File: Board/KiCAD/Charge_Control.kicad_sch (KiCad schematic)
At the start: 56 parts, among them Q1 AON7408, Q10 AON7407, Q2 AON7408, Q3 AON7408, Q4 AON7408, U1 BQ25730RSNR, U3 LTC2943CDD#PBF

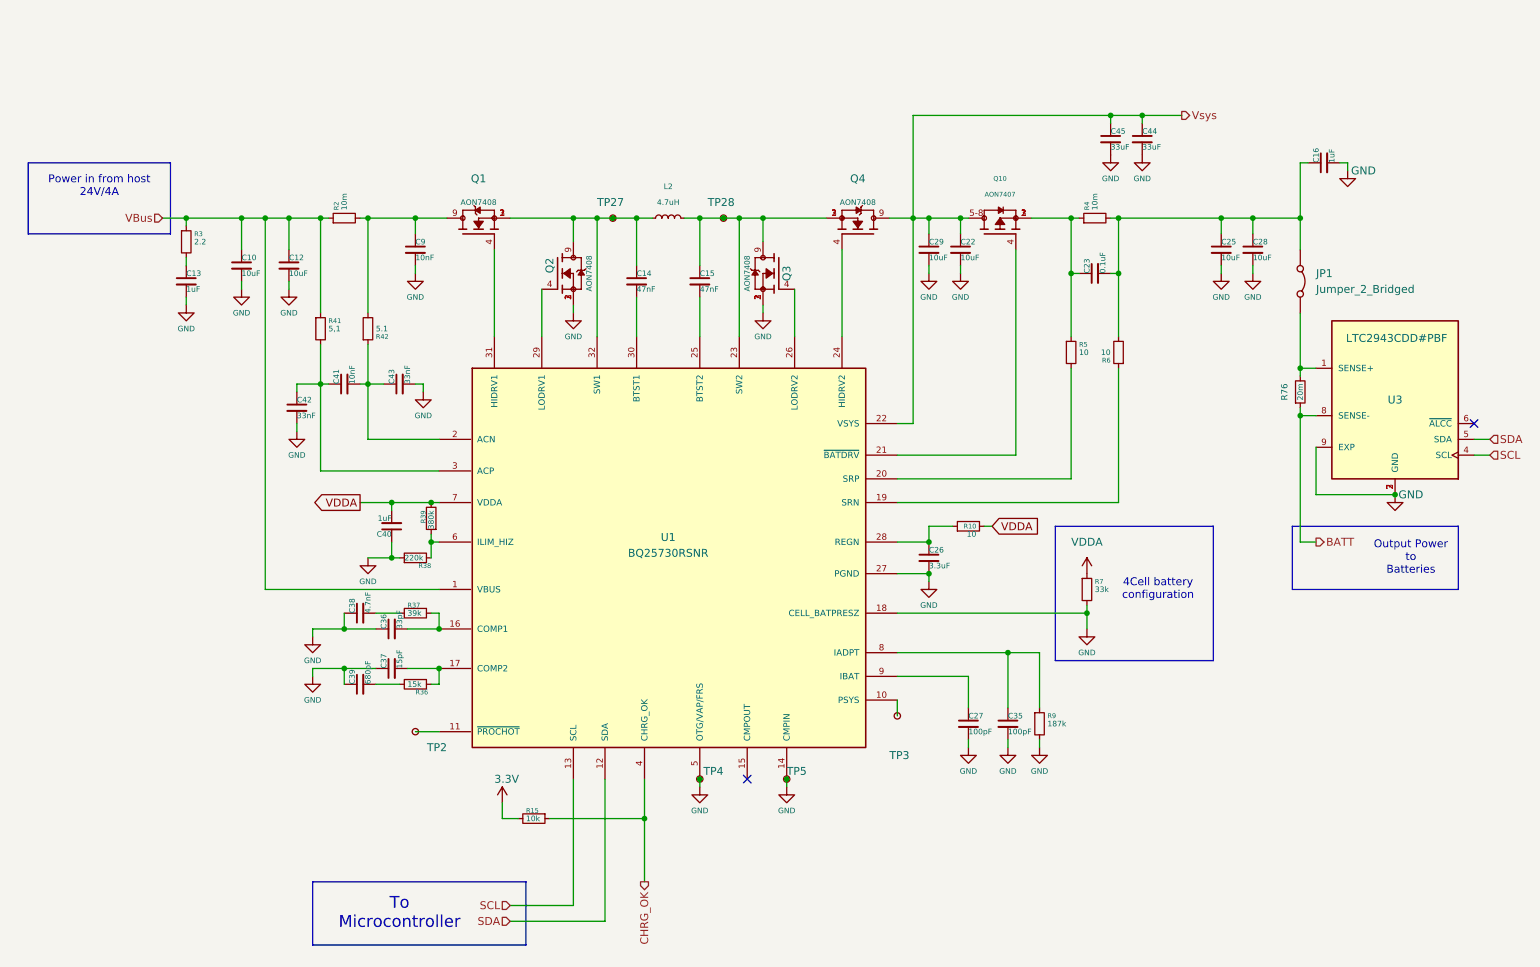
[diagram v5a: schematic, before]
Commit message: Started updating BOM with MFR/MPN
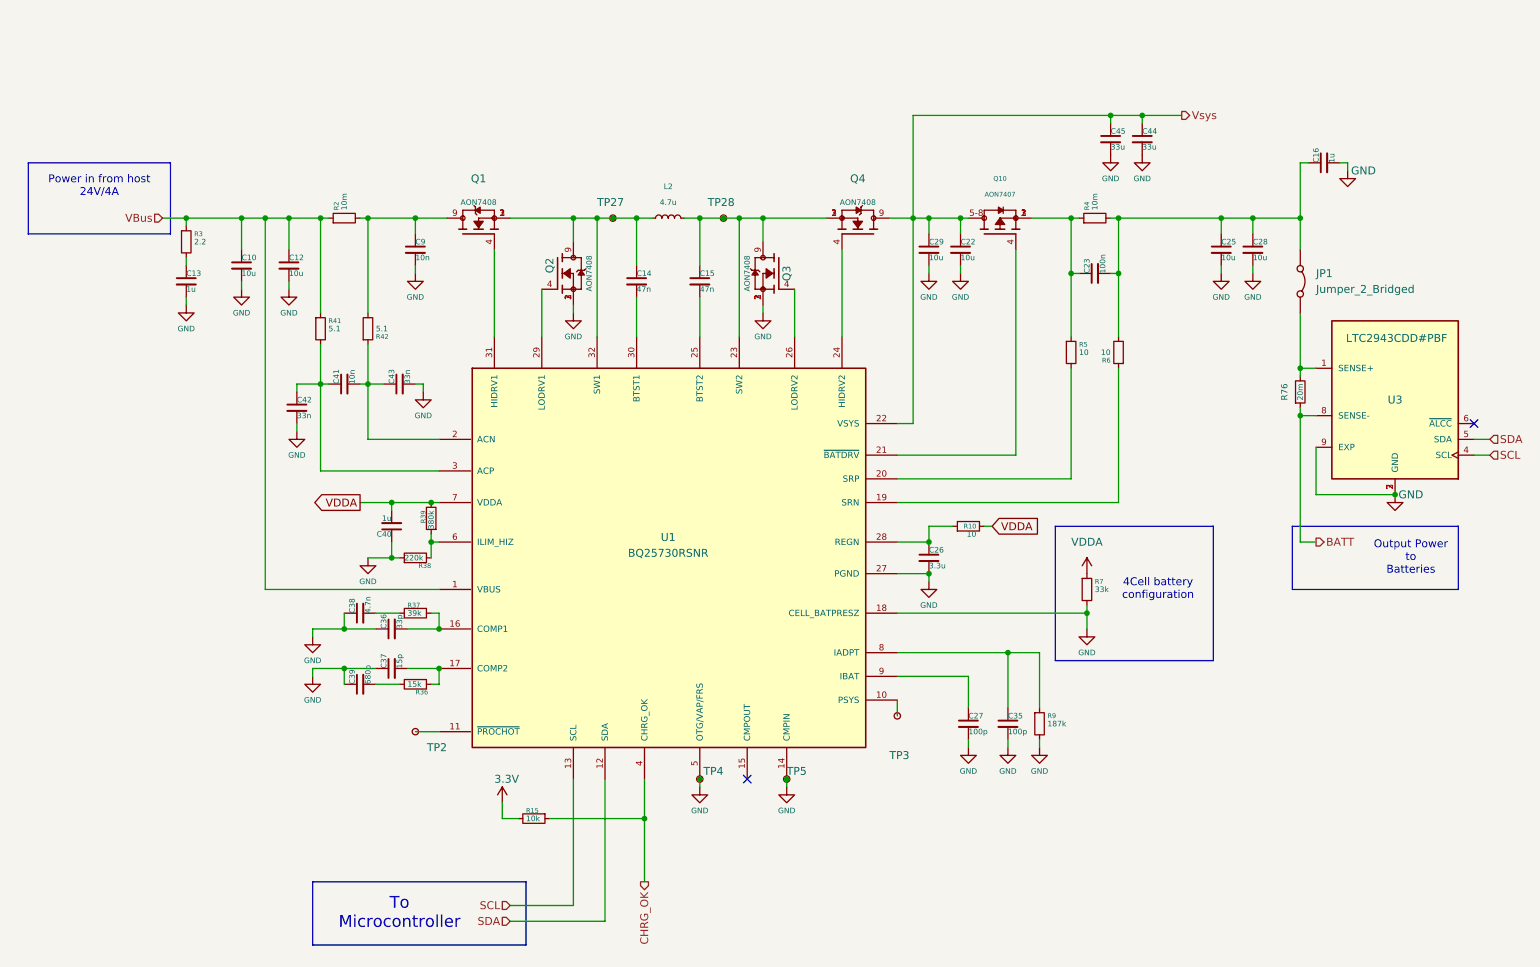
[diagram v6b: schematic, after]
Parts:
- C10, C12, C22, C25, C28, C29: value 10uF -> 10u
- C13, C16, C40: value 1uF -> 1u
- C14, C15: value 47nF -> 47n
- C23: value 0.1uF -> 100n
- C26: value 3.3uF -> 3.3u
- C27, C35: value 100pF -> 100p
- C36: value 33pF -> 33p
- C37: value 15pF -> 15p
- C38: value 4.7nF -> 4.7n
- C39: value 680pF -> 680p
- C41, C9: value 10nF -> 10n
- C42, C43: value 33nF -> 33n
- C44, C45: value 33uF -> 33u
- L2: value 4.7uH -> 4.7u
- Q1, Q2, Q3, Q4: MANUFACTURER Alpha & Omega Semiconductor -> (none); MAXIMUM_PACKAGE_HEIGHT 0.90 mm -> (none); MFR (none) -> Alpha & Omega Semiconductor; PARTREV G -> (none); STANDARD Manufacturer Recommendations -> (none)
- Q10: Availability In Stock -> (none); Check_prices https://www.snapeda.com/parts/AON7407/Alpha/view-part/?ref=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 -> (none); Description_1 P-Channel 20 V 14.5A (Ta), 40A (Tc) 3.1W (Ta), 29W (Tc) Sur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 -> (none); MANUFACTURER Alpha Omega -> (none); MAXIMUM_PACKAGE_HEIGHT 0.9mm -> (none); PARTREV 0 -> (none); Package DFN-8 Alpha &amp; -> (none); Price None -> (none); STANDARD Manufacturer Recommendations -> (none); SnapEDA_Link https://www.snapeda.com/parts/AON7407/Alpha/view-part/?ref=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 -> (none)
- R15: MFR (none) -> Stackpole Electronics Inc; MPN (none) -> RMCF0603FT10K0
- R41: value 5,1 -> 5.1

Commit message: BOM Complete Need a Once Over Check
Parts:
- C10, C12, C22, C25, C28, C29: MFR SAMSUNG -> Samsung Electro-Mechanics; MPN CL31A106KBHNNNE -> 1276-1804-1-ND; Package (none) -> CL31B106KAHNNNE
- C13, C16, C40: MFR (none) -> Aillen; MPN (none) -> 3372-0603B105K100XDTR-ND; Package (none) -> 0603B105K100XD
- C14, C15: MFR (none) -> Murata Electronics; MPN (none) -> 490-4934-1-ND; Package (none) -> GCM188R71H473KA55D
- C23: MFR (none) -> Aillen; MPN (none) -> 3372-0603B104K500XDTR-ND; Package (none) -> 0603B104K500XD
- C26: MFR (none) -> Samsung Electro-Mechanics; MPN (none) -> 1276-1892-1-ND; Package (none) -> CL10A335KP8NNNC
- C27, C35: MFR (none) -> NextGen Components; MPN (none) -> 3372-0603N101J500SDTR-ND; Package (none) -> 0603N101J500SD
- C36, C44, C45: MFR (none) -> Murata Electronics; MPN (none) -> 490-1415-1-ND; Package (none) -> GRM1885C1H330JA01D
- C37: MFR (none) -> KYOCERA AVX; MPN (none) -> 478-600S150JT250XT4KCT-ND; Package (none) -> 600S150JT250XT4K
- C38: MFR (none) -> TDK Corporation; MPN (none) -> 445-6912-1-ND; Package (none) -> CGA3E2C0G1H472J080AA
- C39: MFR (none) -> KEMET; MPN (none) -> 399-C0603C681F5GACTUCT-ND; Package (none) -> C0603C681F5GACTU
- C41, C9: MFR (none) -> Murata Electronics; MPN (none) -> 490-3194-1-ND; Package (none) -> GRM033R71A103KA01D
- C42, C43: MFR (none) -> Murata Electronics; MPN (none) -> 490-8025-1-ND; Package (none) -> GCM188R71H333KA55D
- L2: MFR (none) -> EPCOS - TDK Electronics; MPN (none) -> 495-1805-1-ND; Package (none) -> B82464G4472M000
- Q1, Q2, Q3, Q4: MPN (none) -> 785-1307-1-ND; Package (none) -> AON7408
- Q10: MPN AON7407 -> 785-1306-1-ND; Package (none) -> AON7407
- R10, R5, R6: MFR (none) -> Stackpole Electronics Inc; MPN (none) -> RMCF0603FT10R0CT-ND; Package (none) -> RMCF0603FT10R0
- R15: MPN RMCF0603FT10K0 -> RMCF0603FT10K0CT-ND; Package (none) -> RMCF0603FT10K0
- R2, R4: MFR (none) -> Stackpole Electronics Inc; MPN (none) -> CSR1206FK10L0CT-ND; Package (none) -> CSR1206FK10L0
- R3: MFR (none) -> Stackpole Electronics Inc; MPN (none) -> RMCF1206FT2R20CT-ND; Package (none) -> RMCF1206FT2R20
- R36: MFR (none) -> Stackpole Electronics Inc; MPN (none) -> RMCF0603FT15K0CT-ND; Package (none) -> RMCF0603FT15K0CT-ND
- R37: MFR (none) -> Stackpole Electronics Inc; MPN (none) -> RMCF0603JT39K0CT-ND; Package (none) -> RMCF0603JT39K0
- R38: MFR (none) -> Stackpole Electronics Inc; MPN (none) -> RMCF0603FT220KCT-ND; Package (none) -> RMCF0603FT220K
- R39: MFR (none) -> Stackpole Electronics Inc; MPN (none) -> RMCF0603FT383KCT-ND; Package (none) -> RMCF0603FT383K
- R41, R42: MFR (none) -> Stackpole Electronics Inc; MPN (none) -> RMCF0603FT5R10CT-ND; Package (none) -> RMCF0603FT5R10
- R7: MFR (none) -> Stackpole Electronics Inc; MPN (none) -> RMCF0603FT33K0CT-ND; Package (none) -> RMCF0603FT33K0
- R76: MFR (none) -> Stackpole Electronics Inc; MPN (none) -> CSR1206FK20L0CT-ND; Package (none) -> CSR1206FK20L0
- R9: MFR (none) -> Stackpole Electronics Inc; MPN (none) -> RMCF0603FT187KCT-ND; Package (none) -> RMCF0603FT187K
- U1: Package (none) -> BQ25730RSNR
- U3: Package (none) -> LTC2943CDD#PBF

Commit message: Updated schematic
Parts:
- C26: MFR Samsung Electro-Mechanics -> (none)
- C36: Package GRM1885C1H330JA01D -> (none)
- C42: MFR Murata Electronics -> (none)
- C43: MFR Murata Electronics -> urata Electronics
- L2: MFR EPCOS - TDK Electronics -> (none)
- R3: MPN RMCF1206FT2R20CT-ND -> (none)
